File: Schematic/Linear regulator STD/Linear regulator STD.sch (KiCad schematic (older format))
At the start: 9 parts, among them U1 LM317T

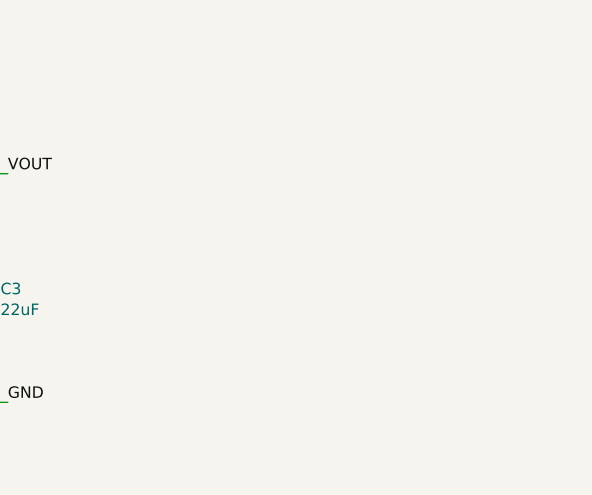
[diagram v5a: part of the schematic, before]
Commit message: TO-220 vertical footprint
added also 1x04 2.54 header
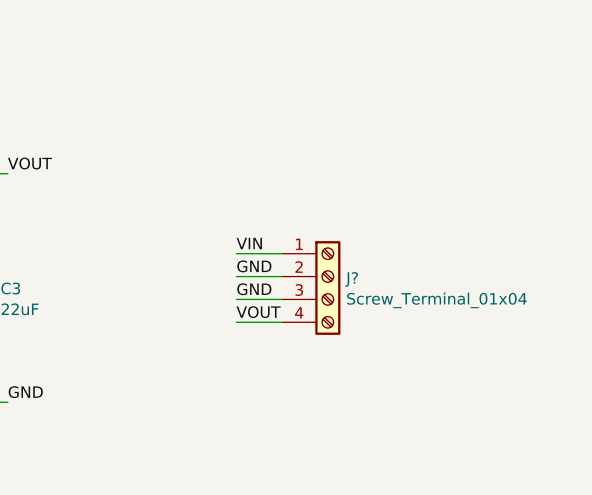
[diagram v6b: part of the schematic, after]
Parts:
- added J?: Screw_Terminal_01x04, Connector_PinSocket_2.54mm:PinSocket_1x04_P2.54mm_Vertical, symbol Connector:Screw_Terminal_01x04
- U1: footprint digikey-footprints:TO-220-3 -> Package_TO_SOT_THT:TO-220-3_Horizontal_TabDown
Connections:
- wire segments 35 -> 39
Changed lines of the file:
@@
 EESchema Schematic File Version 4
+LIBS:Linear regulator STD-cache
 EELAYER 29 0
 EELAYER END
@@
 F 0 "U1" H 5950 3187 60  0000 C CNN
 F 1 "LM317T" H 5950 3081 60  0000 C CNN
-F 2 "digikey-footprints:TO-220-3" H 6150 3100 60  0001 L CNN
+F 2 "Package_TO_SOT_THT:TO-220-3_Horizontal_TabDown" H 6150 3100 60  0001 L CNN
 F 3 "http://www.st.com/content/ccc/resource/technical/document/datasheet/group1/a0/db/e6/9b/6f/9c/45/7b/CD00000455/files/CD00000455.pdf/jcr:content/translations/en.CD00000455.pdf" H 6150 3200 60  0001 L CNN
 F 4 "497-1575-5-ND" H 6150 3300 60  0001 L CNN "Digi-Key_PN"
@@
 Wire Wire Line
 	4950 3900 5350 3900
+$Comp
+L Connector:Screw_Terminal_01x04 J?
+U 1 1 5CD1BDA5
+P 8700 3350
+F 0 "J?" H 8780 3342 50  0000 L CNN
+F 1 "Screw_Terminal_01x04" H 8780 3251 50  0000 L CNN
+F 2 "Connector_PinSocket_2.54mm:PinSocket_1x04_P2.54mm_Vertical" H 8700 3350 50  0001 C CNN
+F 3 "~" H 8700 3350 50  0001 C CNN
+	1    8700 3350
+	1    0    0    -1
+$EndComp
+Wire Wire Line
+	8500 3250 8300 3250
+Wire Wire Line
+	8500 3350 8300 3350
+Wire Wire Line
+	8500 3450 8300 3450
+Wire Wire Line
+	8500 3550 8300 3550
+Text Label 8300 3250 0    50   ~ 0
+VIN
+Text Label 8300 3350 0    50   ~ 0
+GND
+Text Label 8300 3450 0    50   ~ 0
+GND
+Text Label 8300 3550 0    50   ~ 0
+VOUT
 $EndSCHEMATC

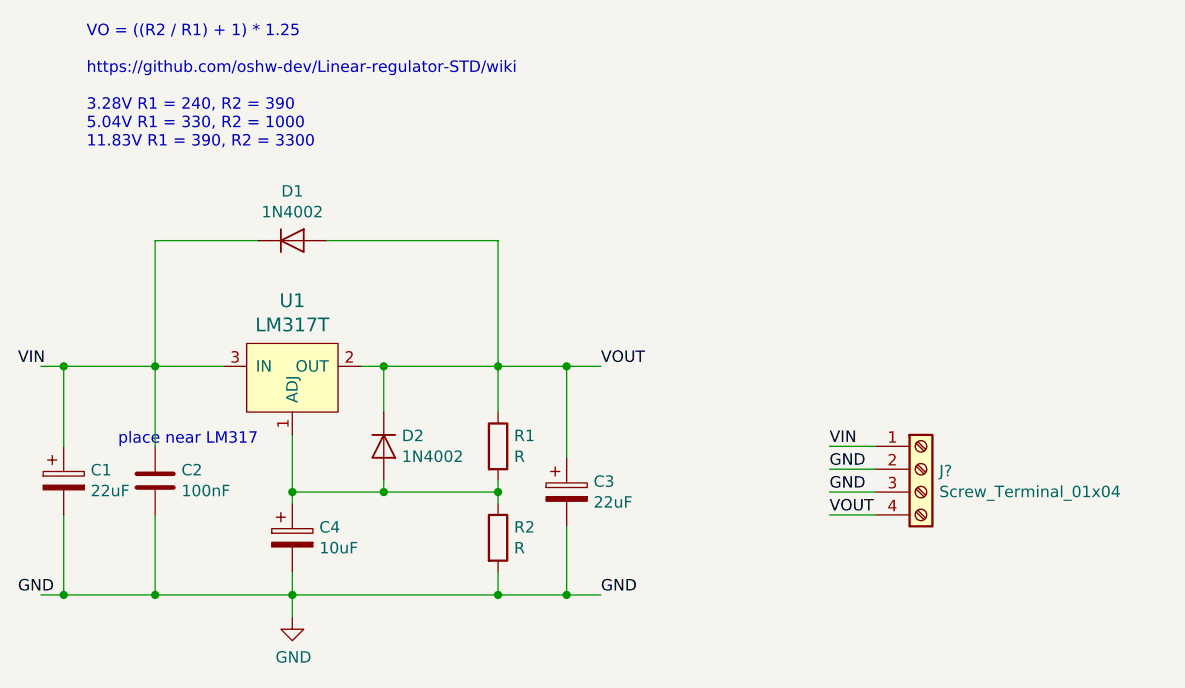
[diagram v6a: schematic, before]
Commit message: label bug
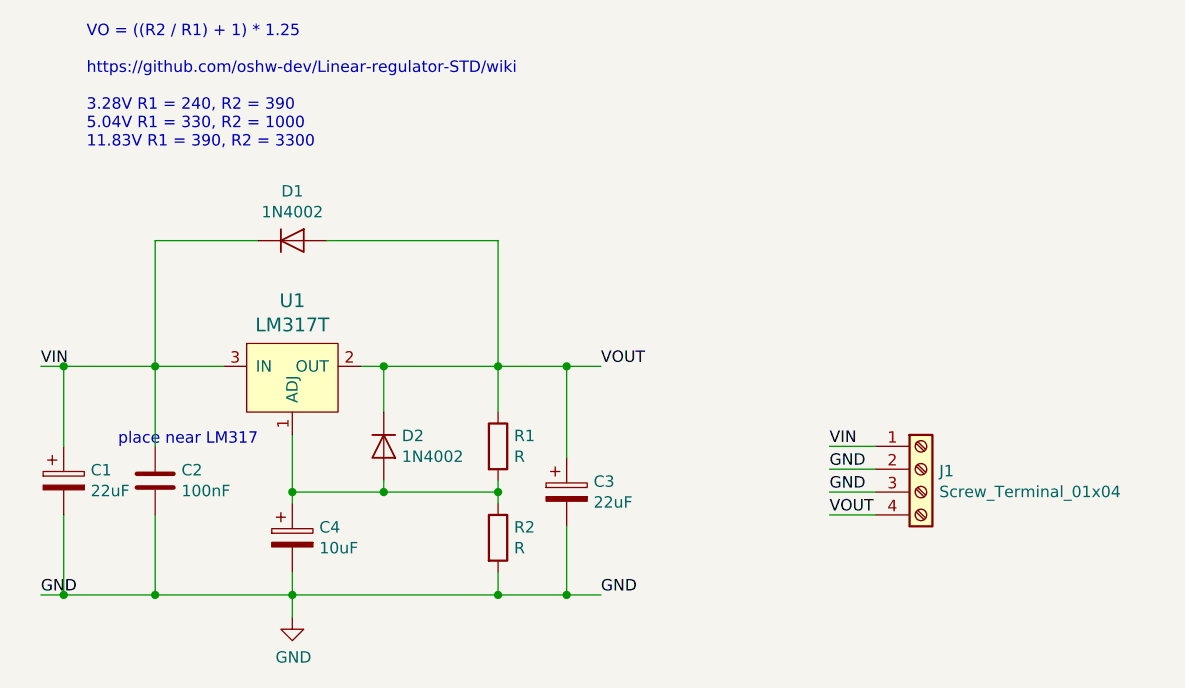
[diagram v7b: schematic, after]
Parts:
- gave numbers to parts that had none: 1
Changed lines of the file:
@@
 Text Label 7300 2900 0    50   ~ 0
 VOUT
-Text Label 4750 2900 0    50   ~ 0
+Text Label 4850 2900 0    50   ~ 0
 VIN
 Text Label 7300 3900 0    50   ~ 0
 GND
-Text Label 4750 3900 0    50   ~ 0
+Text Label 4850 3900 0    50   ~ 0
 GND
 $Comp
@@
 	4950 3900 5350 3900
 $Comp
-L Connector:Screw_Terminal_01x04 J?
+L Connector:Screw_Terminal_01x04 J1
 U 1 1 5CD1BDA5
 P 8700 3350
-F 0 "J?" H 8780 3342 50  0000 L CNN
+F 0 "J1" H 8780 3342 50  0000 L CNN
 F 1 "Screw_Terminal_01x04" H 8780 3251 50  0000 L CNN
 F 2 "Connector_PinSocket_2.54mm:PinSocket_1x04_P2.54mm_Vertical" H 8700 3350 50  0001 C CNN

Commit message: pin header 90 degree update
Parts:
- J1: footprint Connector_PinSocket_2.54mm:PinSocket_1x04_P2.54mm_Vertical -> Connector_PinHeader_2.54mm:PinHeader_1x04_P2.54mm_Horizontal
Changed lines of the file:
@@
 EESchema Schematic File Version 4
-LIBS:Linear regulator STD-cache
 EELAYER 29 0
 EELAYER END
@@
 F 0 "J1" H 8780 3342 50  0000 L CNN
 F 1 "Screw_Terminal_01x04" H 8780 3251 50  0000 L CNN
-F 2 "Connector_PinSocket_2.54mm:PinSocket_1x04_P2.54mm_Vertical" H 8700 3350 50  0001 C CNN
+F 2 "Connector_PinHeader_2.54mm:PinHeader_1x04_P2.54mm_Horizontal" H 8700 3350 50  0001 C CNN
 F 3 "~" H 8700 3350 50  0001 C CNN
 	1    8700 3350
